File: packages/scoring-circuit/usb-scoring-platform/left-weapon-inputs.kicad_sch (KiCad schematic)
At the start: 15 parts, among them J3 LEFT WEAPON A B C, U8 74LVC125APW

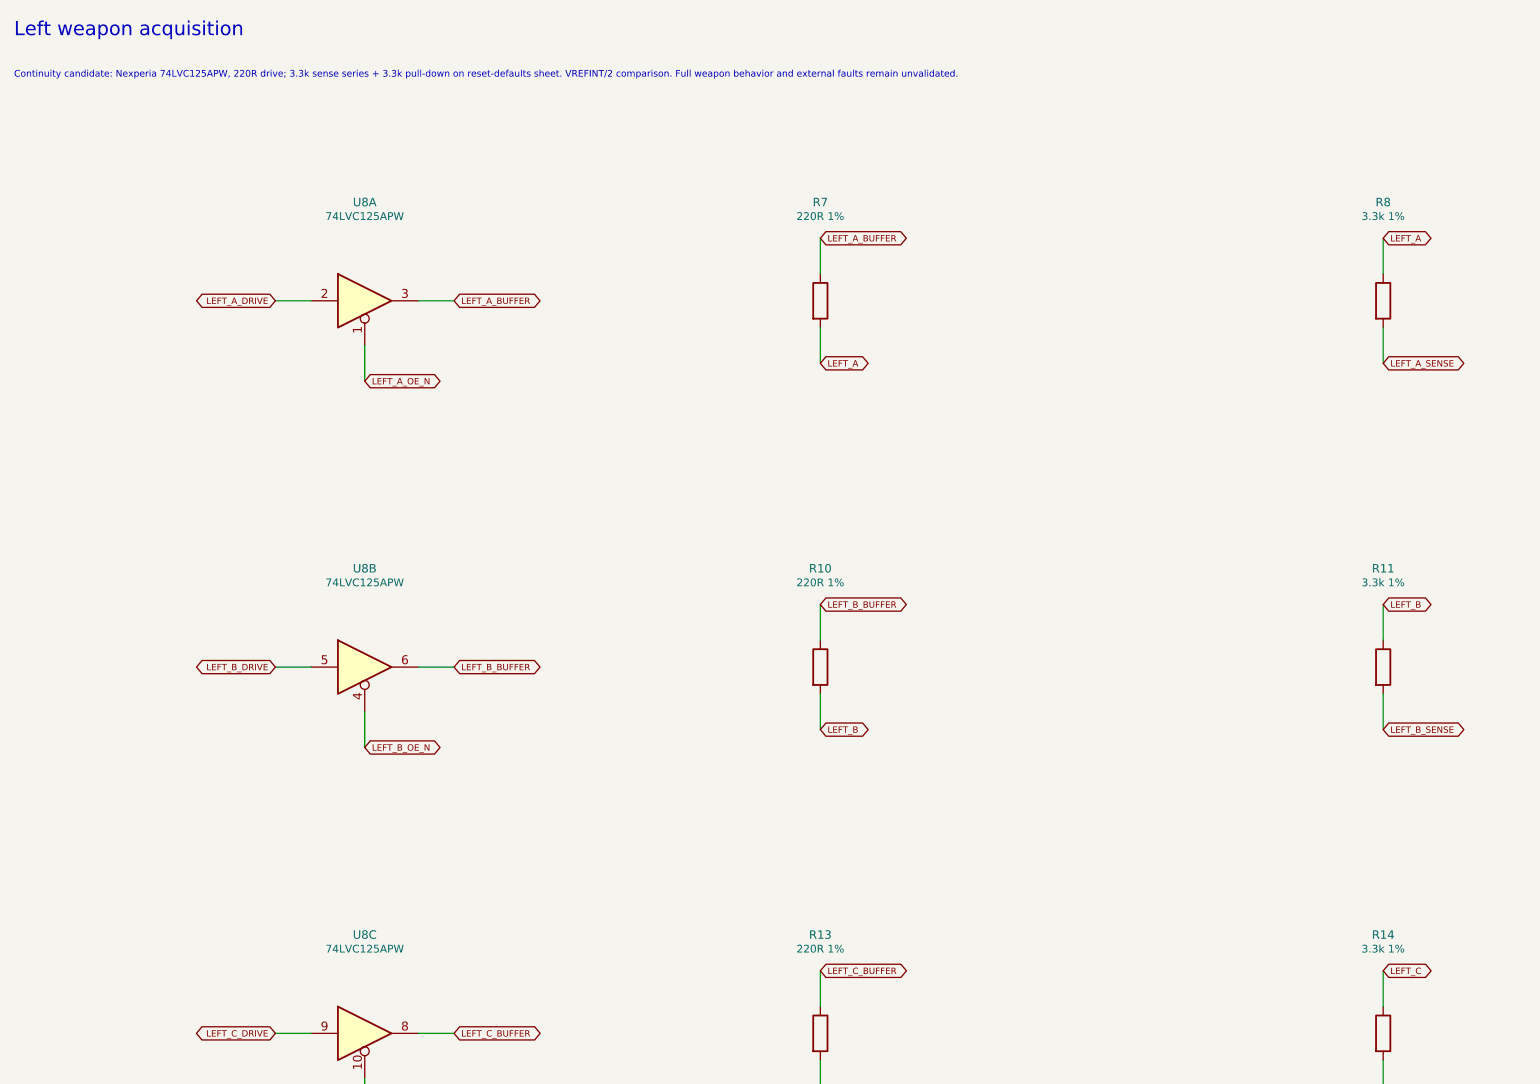
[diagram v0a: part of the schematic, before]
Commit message: fix(scoring): shorten acquisition scan and qualify contact inputs
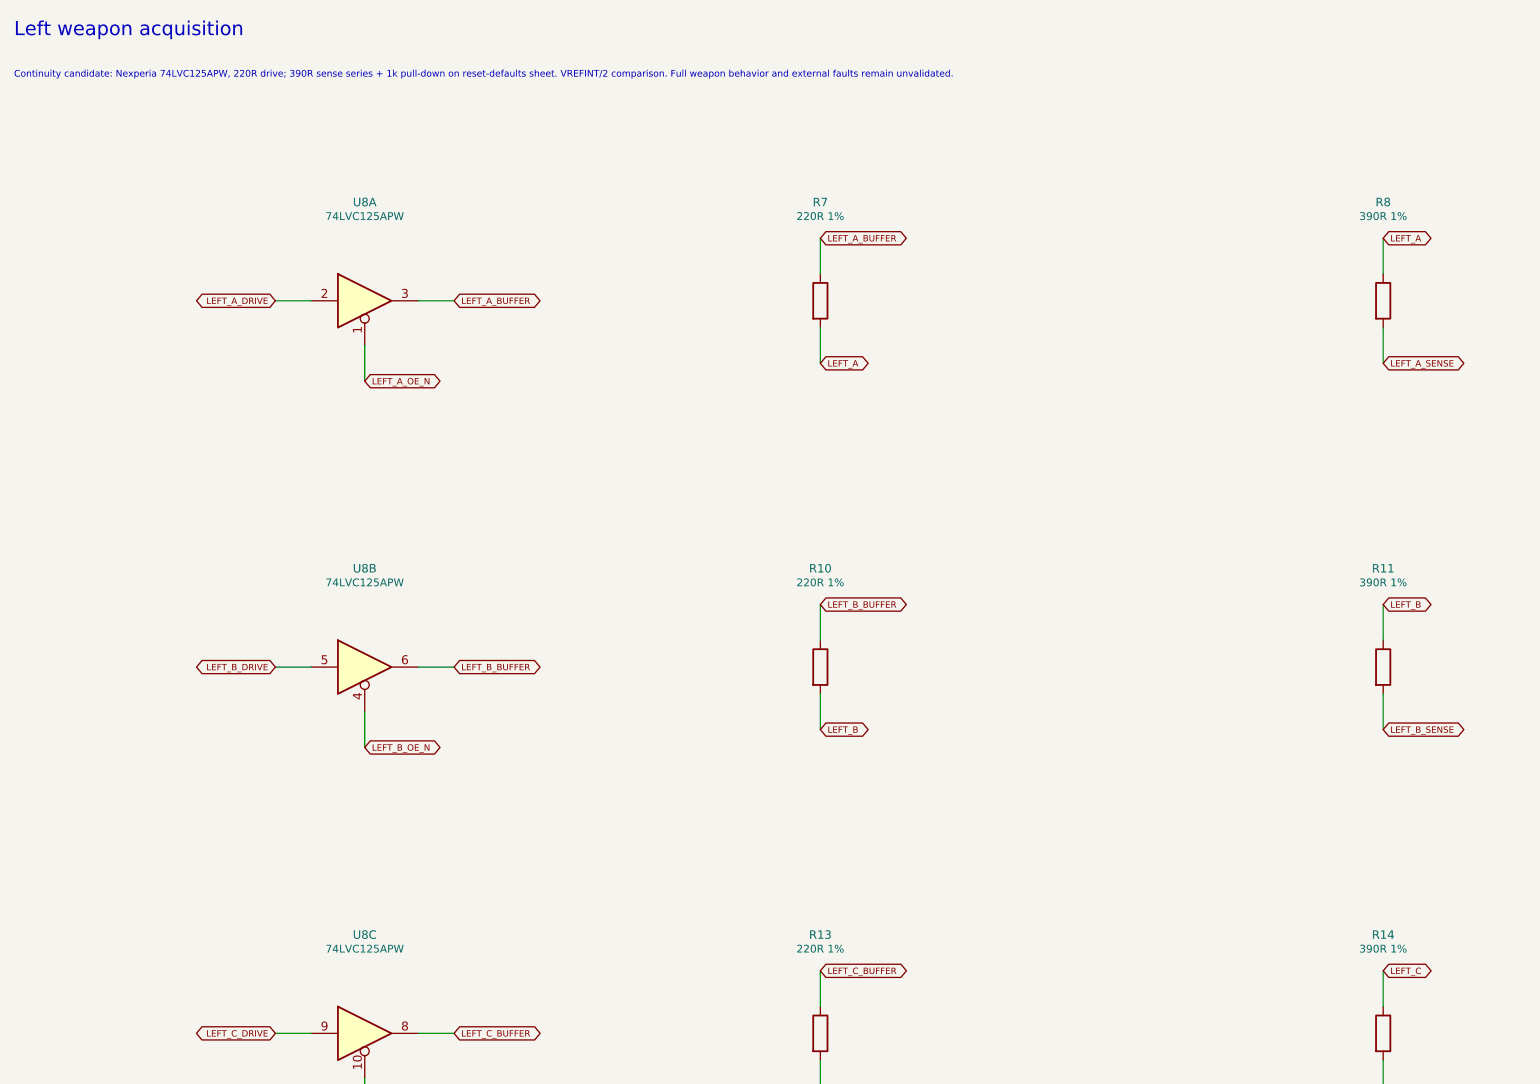
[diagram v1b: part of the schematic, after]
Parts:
- R11, R14, R8: value 3.3k 1% -> 390R 1%; MPN RC0603FR-073K3L -> RC0603FR-07390RL
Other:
- note added: "Continuity candidate: Nexperia 74LVC125APW, 220R drive; 390R sense series + 1k pull-down on reset-defaults sheet. VREFINT/2 comparison. Full weapon behavior and external faults remain unvalidated."
- note removed: "Continuity candidate: Nexperia 74LVC125APW, 220R drive; 3.3k sense series + 3.3k pull-down on reset-defaults sheet. VREFINT/2 comparison. Full weapon behavior and external faults remain unvalidated."

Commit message: fix(scoring-circuit): source stocked bypass and reservoir capacitors
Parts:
- C19: MPN C1608X7R1H104K080AA -> CC0603KRX7R9BB104; Manufacturer TDK -> Yageo
